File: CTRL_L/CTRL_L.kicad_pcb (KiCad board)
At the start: 2 copper layers, 34 x 63.9 mm, 31 parts, among them J1 503480-0540, J2 AYF530365TA, J3 5034801400, J4 503480-0440, U1 74LVC1G08, U2 DRV5033FAxDBZ

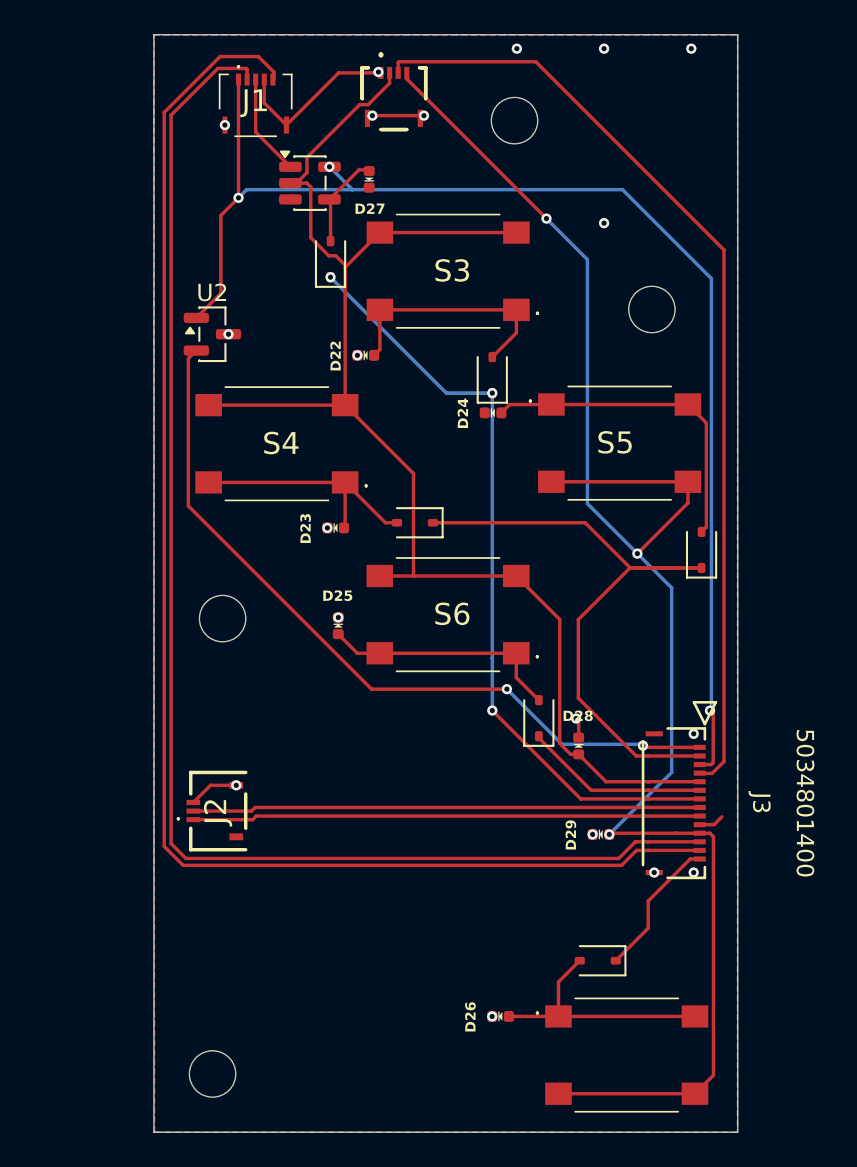
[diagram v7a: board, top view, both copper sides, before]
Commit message: Updated CTRL_L and R to fit new CTRL_Z connector placement
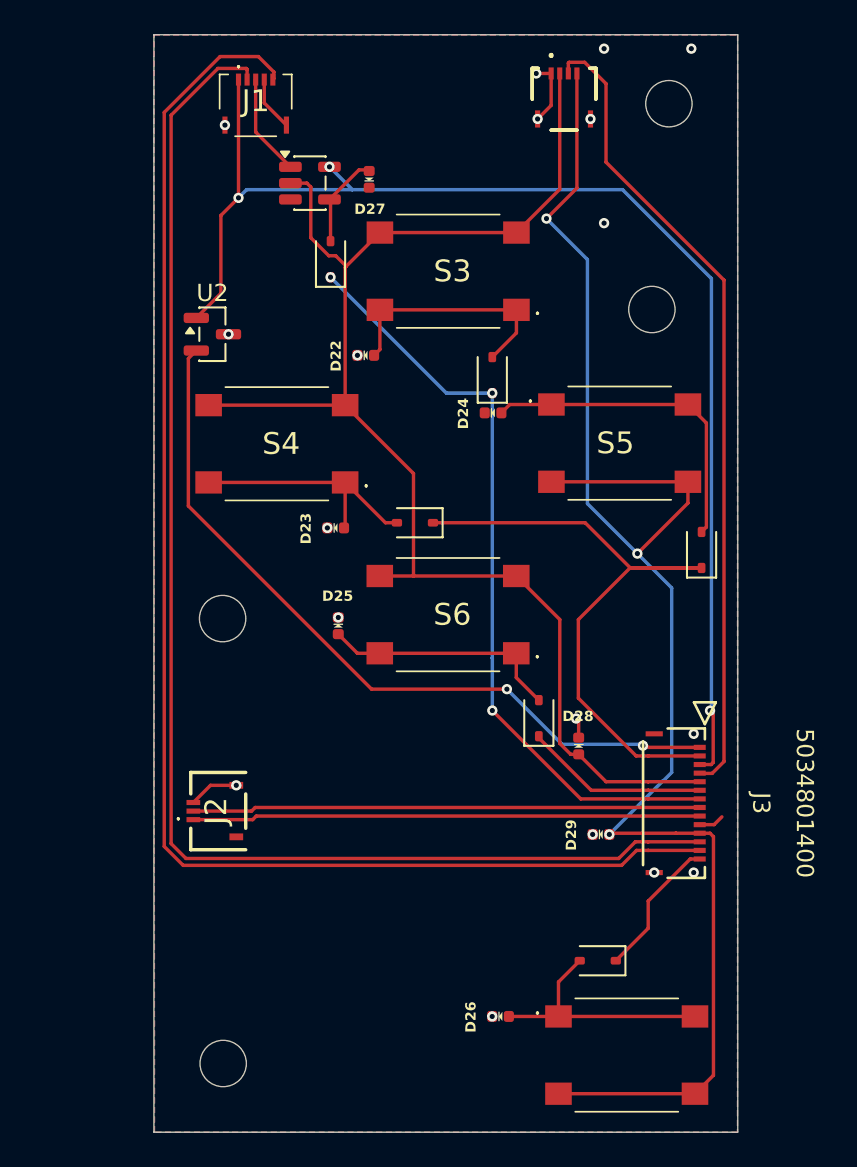
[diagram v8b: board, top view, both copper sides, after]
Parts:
- moved J4 9.91 mm to (155.1, 69.0)
- moved H1 9.04 mm to (161.3, 69.2)
- moved H4 0.87 mm to (135.3, 125.1)
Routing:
- net Row1: track 55.4 -> 47.1 mm
- net GND: track 18.9 -> 12.6 mm, vias 19 -> 18
- net Col2: track 95.1 -> 92.5 mm
- net Col1: track 82.5 -> 83.5 mm
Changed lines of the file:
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@@
 	(footprint "503480-0440:5034800440"
 		(layer "F.Cu")
-		(at 145.24 68.95)
+		(at 155.148 68.983)
 		(descr "503480-0440-2")
 		(tags "Connector")
@@
 	(footprint "MountingHole:MountingHole_2.7mm_M2.5"
 		(layer "F.Cu")
-		(at 134.68 125.75)
+		(at 135.298 125.14)
 		(descr "Mounting Hole 2.7mm, M2.5, no annular, generated by kicad-footprint-generator mountinghole.py")
 		(tags "mountinghole M2.5")
@@
 	(footprint "MountingHole:MountingHole_2.7mm_M2.5"
 		(layer "F.Cu")
-		(at 152.265 70.23)
+		(at 161.255 69.245)
 		(descr "Mounting Hole 2.7mm, M2.5, no annular, generated by kicad-footprint-generator mountinghole.py")
 		(tags "mountinghole M2.5")
@@
 	)
 	(segment
-		(start 144.99 68.05)
-		(end 143.74 69.3)
-		(width 0.2)
-		(layer "F.Cu")
-		(net "Col1")
-	)
-	(segment
 		(start 152.366674 96.75)
 		(end 154.9 99.283326)
@@
 	)
 	(segment
-		(start 139.565552 73.87)
-		(end 139.2125 73.87)
-		(width 0.2)
-		(layer "F.Cu")
-		(net "Col1")
-	)
-	(segment
 		(start 142.4625 78.7125)
 		(end 141.85 78.1)
@@
 	)
 	(segment
-		(start 144.99 67.45)
-		(end 144.99 68.05)
-		(width 0.2)
-		(layer "F.Cu")
-		(net "Col1")
-	)
-	(segment
 		(start 144.425 76.75)
 		(end 152.375 76.75)
@@
 	)
 	(segment
+		(start 154.898 74.227)
+		(end 154.898 67.483)
+		(width 0.2)
+		(layer "F.Cu")
+		(net "Col1")
+	)
+	(segment
 		(start 157.594992 108.729992)
 		(end 160.05 108.729992)
@@
 	)
 	(segment
-		(start 141.45 78.1)
-		(end 140.4 77.05)
+		(start 152.375 76.75)
+		(end 154.898 74.227)
 		(width 0.2)
 		(layer "F.Cu")
@@
 	)
 	(segment
-		(start 140.175 73.260552)
-		(end 139.565552 73.87)
+		(start 141.45 78.1)
+		(end 140.4 77.05)
 		(width 0.2)
 		(layer "F.Cu")
@@
 	)
 	(segment
-		(start 143.74 69.3)
-		(end 143.25 69.3)
-		(width 0.2)
-		(layer "F.Cu")
-		(net "Col1")
-	)
-	(segment
-		(start 143.25 69.3)
-		(end 140.175 72.375)
-		(width 0.2)
-		(layer "F.Cu")
-		(net "Col1")
-	)
-	(segment
-		(start 140.175 72.375)
-		(end 140.175 73.260552)
-		(width 0.2)
-		(layer "F.Cu")
-		(net "Col1")
-	)
-	(segment
 		(start 163.05 108.73001)
 		(end 160.050018 108.73001)
@@
 	)
 	(segment
-		(start 142.02 67.45)
-		(end 138.98 70.49)
-		(width 0.2)
-		(layer "F.Cu")
-		(net "GND")
-	)
-	(segment
 		(start 137.69 69.2)
 		(end 138.98 70.49)
@@
 	)
 	(segment
-		(start 144.49 67.45)
-		(end 142.02 67.45)
-		(width 0.2)
-		(layer "F.Cu")
-		(net "GND")
-	)
-	(segment
 		(start 163.885992 111.230008)
 		(end 164.341 110.775)
@@
 	)
 	(segment
-		(start 143.99 69.94)
-		(end 146.99 69.94)
+		(start 154.398 69.343)
+		(end 153.608 70.133)
 		(width 0.2)
 		(layer "F.Cu")
@@
 	)
 	(segment
-		(start 144.49 67.45)
-		(end 144.389998 67.45)
+		(start 156 105.2)
+		(end 155.85 105.05)
 		(width 0.2)
 		(layer "F.Cu")
@@
 	)
 	(segment
-		(start 156 105.2)
-		(end 155.85 105.05)
+		(start 154.398 67.483)
+		(end 154.398 69.343)
 		(width 0.2)
 		(layer "F.Cu")
@@
 	)
 	(segment
-		(start 144.389998 67.45)
-		(end 144.339998 67.4)
+		(start 154.398 67.483)
+		(end 153.527 67.483)
 		(width 0.2)
 		(layer "F.Cu")
@@
 	)
 	(via
-		(at 157.48 76.2)
+		(at 153.527 67.483)
 		(size 0.6)
 		(drill 0.3)
 		(layers "F.Cu" "B.Cu")
-		(free yes)
 		(net "GND")
 	)
 	(via
-		(at 152.4 66.04)
+		(at 157.48 76.2)
 		(size 0.6)
 		(drill 0.3)
@@
 	)
 	(via
-		(at 146.99 69.94)
+		(at 150.965 122.4)
 		(size 0.6)
 		(drill 0.3)
@@
 	)
 	(via
-		(at 150.965 122.4)
+		(at 156.688 70.133)
 		(size 0.6)
 		(drill 0.3)
@@
 	)
 	(via
-		(at 144.339998 67.4)
+		(at 135.6075 82.67)
 		(size 0.6)
 		(drill 0.3)
@@
 	)
 	(via
-		(at 135.6075 82.67)
+		(at 135.4 70.49)
 		(size 0.6)
 		(drill 0.3)
@@
 	)
 	(via
-		(at 135.4 70.49)
+		(at 153.608 70.133)
 		(size 0.6)
 		(drill 0.3)
@@
 	)
 	(via
-		(at 143.99 69.94)
-		(size 0.6)
-		(drill 0.3)
-		(layers "F.Cu" "B.Cu")
-		(net "GND")
-	)
-	(via
 		(at 155.85 105.05)
 		(size 0.6)
@@
 	)
 	(segment
-		(start 144.49 67.45)
-		(end 144.389998 67.45)
-		(width 0.2)
-		(layer "B.Cu")
-		(net "GND")
-	)
-	(segment
-		(start 144.389998 67.45)
-		(end 144.339998 67.4)
-		(width 0.2)
-		(layer "B.Cu")
-		(net "GND")
-	)
-	(segment
 		(start 154.825 122.4)
 		(end 151.935 122.4)
@@
 	)
 	(segment
-		(start 145.99 67.8)
-		(end 154.125 75.935)
-		(width 0.2)
-		(layer "F.Cu")
-		(net "Col2")
-	)
-	(segment
 		(start 157.785 111.8)
 		(end 157.855009 111.729991)
@@
 	)
 	(segment
-		(start 145.99 67.45)
-		(end 145.99 67.8)
-		(width 0.2)
-		(layer "F.Cu")
-		(net "Col2")
-	)
-	(segment
 		(start 154.412721 91.262721)
 		(end 162.362721 91.262721)
@@
 		(net "Col2")
 	)
+	(segment
+		(start 154.125 75.935)
+		(end 155.898 74.162)
+		(width 0.2)
+		(layer "F.Cu")
+		(net "Col2")
+	)
+	(segment
+		(start 155.898 74.162)
+		(end 155.898 67.483)
+		(width 0.2)
+		(layer "F.Cu")
+		(net "Col2")
+	)
 	(via
 		(at 159.42 95.444)
@@
 	)
 	(segment
-		(start 163.285018 108.245)
-		(end 163.270009 108.229991)
+		(start 155.448 66.833)
+		(end 156.348 66.833)
 		(width 0.2)
 		(layer "F.Cu")
@@
 	)
 	(segment
-		(start 164.464 77.764)
-		(end 164.464 107.554)
+		(start 157.593 72.649)
+		(end 164.464 79.52)
 		(width 0.2)
 		(layer "F.Cu")
@@
 	)
 	(segment
-		(start 145.49 67.45)
-		(end 145.49 66.85)
+		(start 163.773 108.245)
+		(end 163.285018 108.245)
 		(width 0.2)
 		(layer "F.Cu")
@@
 	)
 	(segment
-		(start 163.773 108.245)
-		(end 163.285018 108.245)
+		(start 157.593 68.078)
+		(end 157.593 72.649)
+		(width 0.2)
+		(layer "F.Cu")
+		(net "Row1")
+	)
+	(segment
+		(start 164.464 107.554)
+		(end 163.773 108.245)
 		(width 0.2)
 		(layer "F.Cu")
@@
 	)
 	(segment
-		(start 145.49 66.85)
-		(end 145.54 66.8)
+		(start 164.464 79.52)
+		(end 164.464 107.554)
 		(width 0.2)
 		(layer "F.Cu")
@@
 	)
 	(segment
-		(start 153.5 66.8)
-		(end 164.464 77.764)
+		(start 156.348 66.833)
+		(end 157.593 68.078)
 		(width 0.2)
 		(layer "F.Cu")
@@
 	)
 	(segment
-		(start 145.54 66.8)
-		(end 153.5 66.8)
+		(start 155.398 66.883)
+		(end 155.448 66.833)
 		(width 0.2)
 		(layer "F.Cu")
@@
 	)
 	(segment
-		(start 164.464 107.554)
-		(end 163.773 108.245)
+		(start 155.398 67.483)
+		(end 155.398 66.883)
+		(width 0.2)
+		(layer "F.Cu")
+		(net "Row1")
+	)
+	(segment
+		(start 163.285018 108.245)
+		(end 163.270009 108.229991)
 		(width 0.2)
 		(layer "F.Cu")
@@
 	)
 	(segment
-		(start 137.015678 110.94)
-		(end 133.56 110.94)
+		(start 137.159982 110.23001)
+		(end 163.05 110.23001)
 		(width 0.2)
 		(layer "F.Cu")
-		(net "SL_VIN")
+		(net "SL_VOL")
 	)
 	(segment
-		(start 163.05 110.730009)
-		(end 137.225669 110.730009)
+		(start 136.949992 110.44)
+		(end 137.159982 110.23001)
 		(width 0.2)
 		(layer "F.Cu")
-		(net "SL_VIN")
+		(net "SL_VOL")
 	)
 	(segment
-		(start 137.225669 110.730009)
-		(end 137.015678 110.94)
+		(start 133.56 110.44)
+		(end 136.949992 110.44)
 		(width 0.2)
 		(layer "F.Cu")
-		(net "SL_VIN")
+		(net "SL_VOL")
 	)
 	(segment
-		(start 137.159982 110.23001)
-		(end 163.05 110.23001)
+		(start 137.015678 110.94)
+		(end 133.56 110.94)
 		(width 0.2)
 		(layer "F.Cu")
-		(net "SL_VOL")
+		(net "SL_VIN")
 	)
 	(segment
-		(start 136.949992 110.44)
-		(end 137.159982 110.23001)
+		(start 163.05 110.730009)
+		(end 137.225669 110.730009)
 		(width 0.2)
 		(layer "F.Cu")
-		(net "SL_VOL")
+		(net "SL_VIN")
 	)
 	(segment
-		(start 133.56 110.44)
-		(end 136.949992 110.44)
+		(start 137.225669 110.730009)
+		(end 137.015678 110.94)
 		(width 0.2)
 		(layer "F.Cu")
-		(net "SL_VOL")
+		(net "SL_VIN")
 	)
 	(zone
